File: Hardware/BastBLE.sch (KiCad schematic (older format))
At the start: 35 parts, among them J1 Battery, J2 SWD, J3 Conn_left, J4 Conn_right, P1 USB_C_Plug_USB2.0, Q1 DMG3415U-7, SW1 RESET, U1 AP2112K-3.3, U2 E73-2G4M08S1C, U3 MCP73831-2-OT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

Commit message: Manf#
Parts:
- C1, C2, C3, C4, C5, C6, C7, C8, D2, D3, SW1: manf# (none) -> -
- C10, C9: manf# (none) -> 06035A220JAT4A
- D1: manf# (none) -> MBR120VLSFT3G
- P1: manf# (none) -> MLJ1608WR16JT000
- Q1: manf# (none) -> DMG3415U-7
- R1, R2, R5, R6: manf# (none) -> CRCW0603100KFKEAC
- R3: manf# (none) -> SFR03EZPF4701
- R4, R7: manf# (none) -> RC0603FR-131K27L
- R8, R9: manf# (none) -> CRCW06035K10FKEAC
- U1: manf# (none) -> AP2112K-3.3TRG1
- U3: manf# (none) -> MCP73831-3-OT
- U4: manf# (none) -> W25Q16JVSNIQ
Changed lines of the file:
@@
 EESchema Schematic File Version 4
+LIBS:BastBLE-cache
 EELAYER 30 0
 EELAYER END
@@
 F 2 "Package_TO_SOT_SMD:SOT-23-5" H 1965 6325 50  0001 C CNN
 F 3 "https://www.diodes.com/assets/Datasheets/AP2112.pdf" H 1965 6100 50  0001 C CNN
+F 4 "AP2112K-3.3TRG1" H 1965 6000 50  0001 C CNN "manf#"
 	1    1965 6000
 	1    0    0    -1
@@
 F 2 "Resistor_SMD:R_0603_1608Metric_Pad1.05x0.95mm_HandSolder" H 1490 6040 50  0001 C CNN
 F 3 "~" H 1490 6040 50  0001 C CNN
+F 4 "CRCW0603100KFKEAC" H 1490 6040 50  0001 C CNN "manf#"
 	1    1490 6040
 	1    0    0    -1
@@
 F 2 "Resistor_SMD:R_0603_1608Metric_Pad1.05x0.95mm_HandSolder" H 845 6075 50  0001 C CNN
 F 3 "~" H 845 6075 50  0001 C CNN
+F 4 "CRCW0603100KFKEAC" H 845 6075 50  0001 C CNN "manf#"
 	1    845  6075
 	1    0    0    -1
@@
 F 2 "Diode_SMD:D_SOD-123F" H 1055 5725 50  0001 C CNN
 F 3 "http://www.onsemi.com/pub_link/Collateral/MBR340-D.PDF" H 1055 5900 50  0001 C CNN
+F 4 "MBR120VLSFT3G" H 1055 5900 50  0001 C CNN "manf#"
 	1    1055 5900
 	-1   0    0    1
@@
 F 2 "Capacitor_SMD:C_0603_1608Metric_Pad1.05x0.95mm_HandSolder" H 1290 6070 50  0001 C CNN
 F 3 "~" H 1290 6070 50  0001 C CNN
+F 4 "-" H 1290 6070 50  0001 C CNN "manf#"
 	1    1290 6070
 	1    0    0    -1
@@
 F 2 "Capacitor_SMD:C_0603_1608Metric_Pad1.05x0.95mm_HandSolder" H 2390 6030 50  0001 C CNN
 F 3 "~" H 2390 6030 50  0001 C CNN
+F 4 "-" H 2390 6030 50  0001 C CNN "manf#"
 	1    2390 6030
 	1    0    0    -1
@@
 F 2 "Resistor_SMD:R_0603_1608Metric_Pad1.05x0.95mm_HandSolder" H 4720 865 50  0001 C CNN
 F 3 "~" H 4720 865 50  0001 C CNN
+F 4 "RC0603FR-131K27L" H 4720 865 50  0001 C CNN "manf#"
 	1    4720 865
 	1    0    0    -1
@@
 F 2 "LED_SMD:LED_0805_2012Metric" H 4720 1170 50  0001 C CNN
 F 3 "~" H 4720 1170 50  0001 C CNN
+F 4 "-" H 4720 1170 50  0001 C CNN "manf#"
 	1    4720 1170
 	0    -1   -1   0
@@
 F 2 "Resistor_SMD:R_0603_1608Metric_Pad1.05x0.95mm_HandSolder" H 4720 6695 50  0001 C CNN
 F 3 "~" H 4720 6695 50  0001 C CNN
+F 4 "CRCW0603100KFKEAC" H 4720 6695 50  0001 C CNN "manf#"
 	1    4720 6695
 	1    0    0    -1
@@
 F 2 "Resistor_SMD:R_0603_1608Metric_Pad1.05x0.95mm_HandSolder" H 4720 7020 50  0001 C CNN
 F 3 "~" H 4720 7020 50  0001 C CNN
+F 4 "CRCW0603100KFKEAC" H 4720 7020 50  0001 C CNN "manf#"
 	1    4720 7020
 	1    0    0    -1
@@
 F 2 "Connectors_ElectronicCats:C393939" H 5285 3120 50  0001 C CNN
 F 3 "https://www.usb.org/sites/default/files/documents/usb_type-c.zip" H 5285 3120 50  0001 C CNN
+F 4 "MLJ1608WR16JT000" H 5135 3120 50  0001 C CNN "manf#"
 	1    5135 3120
 	1    0    0    -1
@@
 F 2 "Package_SO:SOIC-8_5.23x5.23mm_P1.27mm" H 8865 5500 50  0001 C CNN
 F 3 "http://www.winbond.com/resource-files/w25q32jv%20revg%2003272018%20plus.pdf" H 8865 5500 50  0001 C CNN
+F 4 "W25Q16JVSNIQ" H 8865 5500 50  0001 C CNN "manf#"
 	1    8865 5500
 	1    0    0    -1
@@
 F 2 "Capacitor_SMD:C_0603_1608Metric_Pad1.05x0.95mm_HandSolder" H 5400 1080 50  0001 C CNN
 F 3 "~" H 5400 1080 50  0001 C CNN
+F 4 "-" H 5400 1080 50  0001 C CNN "manf#"
 	1    5400 1080
 	1    0    0    -1
@@
 F 2 "Capacitor_SMD:C_0603_1608Metric_Pad1.05x0.95mm_HandSolder" H 5740 1075 50  0001 C CNN
 F 3 "~" H 5740 1075 50  0001 C CNN
+F 4 "-" H 5740 1075 50  0001 C CNN "manf#"
 	1    5740 1075
 	1    0    0    -1
@@
 F 2 "Capacitor_SMD:C_0603_1608Metric_Pad1.05x0.95mm_HandSolder" H 6005 1085 50  0001 C CNN
 F 3 "~" H 6005 1085 50  0001 C CNN
+F 4 "-" H 6005 1085 50  0001 C CNN "manf#"
 	1    6005 1085
 	1    0    0    -1
@@
 F 2 "Capacitor_SMD:C_0603_1608Metric_Pad1.05x0.95mm_HandSolder" H 6265 1095 50  0001 C CNN
 F 3 "~" H 6265 1095 50  0001 C CNN
+F 4 "-" H 6265 1095 50  0001 C CNN "manf#"
 	1    6265 1095
 	1    0    0    -1
@@
 F 2 "Capacitor_SMD:C_0603_1608Metric_Pad1.05x0.95mm_HandSolder" H 6535 1095 50  0001 C CNN
 F 3 "~" H 6535 1095 50  0001 C CNN
+F 4 "-" H 6535 1095 50  0001 C CNN "manf#"
 	1    6535 1095
 	1    0    0    -1
@@
 F 2 "Button_Switch_SMD:SW_SPST_TL3342" H 7380 1295 50  0001 C CNN
 F 3 "TS-1185EC-C-D-B" H 7380 1295 50  0001 C CNN
+F 4 "-" H 7380 1095 50  0001 C CNN "manf#"
 	1    7380 1095
 	1    0    0    -1
@@
 F 2 "Resistor_SMD:R_0603_1608Metric_Pad1.05x0.95mm_HandSolder" H 5915 2720 50  0001 C CNN
 F 3 "~" H 5915 2720 50  0001 C CNN
+F 4 "CRCW06035K10FKEAC" H 5915 2720 50  0001 C CNN "manf#"
 	1    5915 2720
 	0    1    1    0
@@
 F 2 "Resistor_SMD:R_0603_1608Metric_Pad1.05x0.95mm_HandSolder" H 5915 2820 50  0001 C CNN
 F 3 "~" H 5915 2820 50  0001 C CNN
+F 4 "CRCW06035K10FKEAC" H 5915 2820 50  0001 C CNN "manf#"
 	1    5915 2820
 	0    1    1    0
@@
 F 2 "Package_TO_SOT_SMD:SOT-23" H 1390 5740 50  0001 C CNN
 F 3 "~" H 1190 5640 50  0001 C CNN
+F 4 "DMG3415U-7" H 1190 5640 50  0001 C CNN "manf#"
 	1    1190 5640
 	1    0    0    -1
@@
 F 2 "Capacitor_SMD:C_0603_1608Metric_Pad1.05x0.95mm_HandSolder" H 4745 5035 50  0001 C CNN
 F 3 "~" H 4745 5035 50  0001 C CNN
+F 4 "-" H 4745 5035 50  0001 C CNN "manf#"
 	1    4745 5035
 	1    0    0    -1
@@
 F 2 "Resistor_SMD:R_0603_1608Metric_Pad1.05x0.95mm_HandSolder" H 3745 5505 50  0001 C CNN
 F 3 "~" H 3745 5505 50  0001 C CNN
+F 4 "SFR03EZPF4701" H 3745 5505 50  0001 C CNN "manf#"
 	1    3745 5505
 	1    0    0    -1
@@
 F 2 "Resistor_SMD:R_0603_1608Metric_Pad1.05x0.95mm_HandSolder" H 4840 5405 50  0001 C CNN
 F 3 "~" H 4840 5405 50  0001 C CNN
+F 4 "RC0603FR-131K27L" H 4840 5405 50  0001 C CNN "manf#"
 	1    4840 5405
 	0    1    1    0
@@
 F 2 "LED_SMD:LED_0805_2012Metric" H 5185 5405 50  0001 C CNN
 F 3 "~" H 5185 5405 50  0001 C CNN
+F 4 "-" H 5185 5405 50  0001 C CNN "manf#"
 	1    5185 5405
 	1    0    0    -1
@@
 F 2 "Package_TO_SOT_SMD:SOT-23-5" H 4320 5055 50  0001 L CIN
 F 3 "http://ww1.microchip.com/downloads/en/DeviceDoc/20001984g.pdf" H 4120 5255 50  0001 C CNN
+F 4 "MCP73831-3-OT" H 4270 5305 50  0001 C CNN "manf#"
 	1    4270 5305
 	1    0    0    -1
@@
 F 2 "Capacitor_SMD:C_0603_1608Metric_Pad1.05x0.95mm_HandSolder" H 1160 2365 50  0001 C CNN
 F 3 "~" H 1160 2365 50  0001 C CNN
+F 4 "06035A220JAT4A" H 1160 2365 50  0001 C CNN "manf#"
 	1    1160 2365
 	0    1    1    0
@@
 F 2 "Capacitor_SMD:C_0603_1608Metric_Pad1.05x0.95mm_HandSolder" H 1160 2030 50  0001 C CNN
 F 3 "~" H 1160 2030 50  0001 C CNN
+F 4 "06035A220JAT4A" H 1160 2030 50  0001 C CNN "manf#"
 	1    1160 2030
 	0    1    1    0

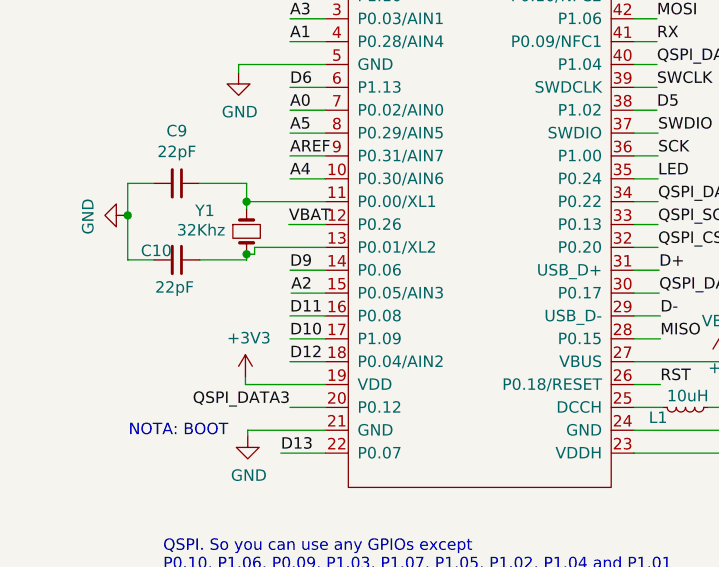
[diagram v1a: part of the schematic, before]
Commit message: VBA and D12 exchanged and routed.
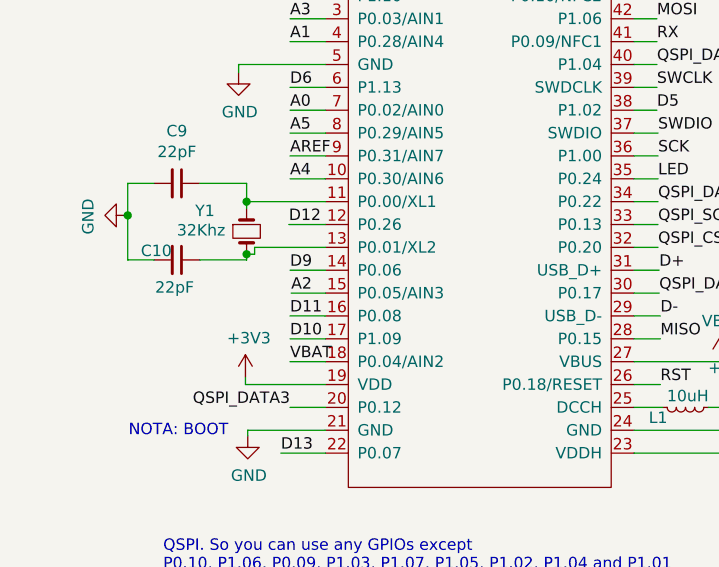
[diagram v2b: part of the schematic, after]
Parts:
- C1, C2, C3, C4, C5, C6, C7, C8, D2, D3, SW1: manf# - -> (none)
- C10, C9: manf# 06035A220JAT4A -> (none)
- D1: manf# MBR120VLSFT3G -> (none)
- P1: manf# MLJ1608WR16JT000 -> (none)
- Q1: manf# DMG3415U-7 -> (none)
- R1, R2, R5, R6: manf# CRCW0603100KFKEAC -> (none)
- R3: manf# SFR03EZPF4701 -> (none)
- R4, R7: manf# RC0603FR-131K27L -> (none)
- R8, R9: manf# CRCW06035K10FKEAC -> (none)
- U1: manf# AP2112K-3.3TRG1 -> (none)
- U3: manf# MCP73831-3-OT -> (none)
- U4: manf# W25Q16JVSNIQ -> (none)
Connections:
- net D12: now also U2.12 (P0.26); no longer U2.18 (P0.04/AIN2)
- net VBAT: now also U2.18 (P0.04/AIN2); no longer U2.12 (P0.26)
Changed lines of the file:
@@
 EESchema Schematic File Version 4
-LIBS:BastBLE-cache
 EELAYER 30 0
 EELAYER END
@@
 F 2 "Package_TO_SOT_SMD:SOT-23-5" H 1965 6325 50  0001 C CNN
 F 3 "https://www.diodes.com/assets/Datasheets/AP2112.pdf" H 1965 6100 50  0001 C CNN
-F 4 "AP2112K-3.3TRG1" H 1965 6000 50  0001 C CNN "manf#"
 	1    1965 6000
 	1    0    0    -1
@@
 F 2 "Resistor_SMD:R_0603_1608Metric_Pad1.05x0.95mm_HandSolder" H 1490 6040 50  0001 C CNN
 F 3 "~" H 1490 6040 50  0001 C CNN
-F 4 "CRCW0603100KFKEAC" H 1490 6040 50  0001 C CNN "manf#"
 	1    1490 6040
 	1    0    0    -1
@@
 RX
 Text Label 1655 2810 0    50   ~ 0
-D12
+VBAT
 Wire Wire Line
 	1615 3210 1810 3210
@@
 F 2 "Resistor_SMD:R_0603_1608Metric_Pad1.05x0.95mm_HandSolder" H 845 6075 50  0001 C CNN
 F 3 "~" H 845 6075 50  0001 C CNN
-F 4 "CRCW0603100KFKEAC" H 845 6075 50  0001 C CNN "manf#"
 	1    845  6075
 	1    0    0    -1
@@
 F 2 "Diode_SMD:D_SOD-123F" H 1055 5725 50  0001 C CNN
 F 3 "http://www.onsemi.com/pub_link/Collateral/MBR340-D.PDF" H 1055 5900 50  0001 C CNN
-F 4 "MBR120VLSFT3G" H 1055 5900 50  0001 C CNN "manf#"
 	1    1055 5900
 	-1   0    0    1
@@
 F 2 "Capacitor_SMD:C_0603_1608Metric_Pad1.05x0.95mm_HandSolder" H 1290 6070 50  0001 C CNN
 F 3 "~" H 1290 6070 50  0001 C CNN
-F 4 "-" H 1290 6070 50  0001 C CNN "manf#"
 	1    1290 6070
 	1    0    0    -1
@@
 F 2 "Capacitor_SMD:C_0603_1608Metric_Pad1.05x0.95mm_HandSolder" H 2390 6030 50  0001 C CNN
 F 3 "~" H 2390 6030 50  0001 C CNN
-F 4 "-" H 2390 6030 50  0001 C CNN "manf#"
 	1    2390 6030
 	1    0    0    -1
@@
 F 2 "Resistor_SMD:R_0603_1608Metric_Pad1.05x0.95mm_HandSolder" H 4720 865 50  0001 C CNN
 F 3 "~" H 4720 865 50  0001 C CNN
-F 4 "RC0603FR-131K27L" H 4720 865 50  0001 C CNN "manf#"
 	1    4720 865
 	1    0    0    -1
@@
 F 2 "LED_SMD:LED_0805_2012Metric" H 4720 1170 50  0001 C CNN
 F 3 "~" H 4720 1170 50  0001 C CNN
-F 4 "-" H 4720 1170 50  0001 C CNN "manf#"
 	1    4720 1170
 	0    -1   -1   0
@@
 F 2 "Resistor_SMD:R_0603_1608Metric_Pad1.05x0.95mm_HandSolder" H 4720 6695 50  0001 C CNN
 F 3 "~" H 4720 6695 50  0001 C CNN
-F 4 "CRCW0603100KFKEAC" H 4720 6695 50  0001 C CNN "manf#"
 	1    4720 6695
 	1    0    0    -1
@@
 F 2 "Resistor_SMD:R_0603_1608Metric_Pad1.05x0.95mm_HandSolder" H 4720 7020 50  0001 C CNN
 F 3 "~" H 4720 7020 50  0001 C CNN
-F 4 "CRCW0603100KFKEAC" H 4720 7020 50  0001 C CNN "manf#"
 	1    4720 7020
 	1    0    0    -1
@@
 Wire Wire Line
 	4720 6855 4720 6795
-Text Label 1650 2210 0    50   ~ 0
-VBAT
 Text Label 4905 6855 0    50   ~ 0
 VBAT
@@
 F 2 "Connectors_ElectronicCats:C393939" H 5285 3120 50  0001 C CNN
 F 3 "https://www.usb.org/sites/default/files/documents/usb_type-c.zip" H 5285 3120 50  0001 C CNN
-F 4 "MLJ1608WR16JT000" H 5135 3120 50  0001 C CNN "manf#"
 	1    5135 3120
 	1    0    0    -1
@@
 F 2 "Package_SO:SOIC-8_5.23x5.23mm_P1.27mm" H 8865 5500 50  0001 C CNN
 F 3 "http://www.winbond.com/resource-files/w25q32jv%20revg%2003272018%20plus.pdf" H 8865 5500 50  0001 C CNN
-F 4 "W25Q16JVSNIQ" H 8865 5500 50  0001 C CNN "manf#"
 	1    8865 5500
 	1    0    0    -1
@@
 F 2 "Capacitor_SMD:C_0603_1608Metric_Pad1.05x0.95mm_HandSolder" H 5400 1080 50  0001 C CNN
 F 3 "~" H 5400 1080 50  0001 C CNN
-F 4 "-" H 5400 1080 50  0001 C CNN "manf#"
 	1    5400 1080
 	1    0    0    -1
@@
 F 2 "Capacitor_SMD:C_0603_1608Metric_Pad1.05x0.95mm_HandSolder" H 5740 1075 50  0001 C CNN
 F 3 "~" H 5740 1075 50  0001 C CNN
-F 4 "-" H 5740 1075 50  0001 C CNN "manf#"
 	1    5740 1075
 	1    0    0    -1
@@
 F 2 "Capacitor_SMD:C_0603_1608Metric_Pad1.05x0.95mm_HandSolder" H 6005 1085 50  0001 C CNN
 F 3 "~" H 6005 1085 50  0001 C CNN
-F 4 "-" H 6005 1085 50  0001 C CNN "manf#"
 	1    6005 1085
 	1    0    0    -1
@@
 F 2 "Capacitor_SMD:C_0603_1608Metric_Pad1.05x0.95mm_HandSolder" H 6265 1095 50  0001 C CNN
 F 3 "~" H 6265 1095 50  0001 C CNN
-F 4 "-" H 6265 1095 50  0001 C CNN "manf#"
 	1    6265 1095
 	1    0    0    -1
@@
 F 2 "Capacitor_SMD:C_0603_1608Metric_Pad1.05x0.95mm_HandSolder" H 6535 1095 50  0001 C CNN
 F 3 "~" H 6535 1095 50  0001 C CNN
-F 4 "-" H 6535 1095 50  0001 C CNN "manf#"
 	1    6535 1095
 	1    0    0    -1
@@
 F 2 "Button_Switch_SMD:SW_SPST_TL3342" H 7380 1295 50  0001 C CNN
 F 3 "TS-1185EC-C-D-B" H 7380 1295 50  0001 C CNN
-F 4 "-" H 7380 1095 50  0001 C CNN "manf#"
 	1    7380 1095
 	1    0    0    -1
@@
 F 2 "Resistor_SMD:R_0603_1608Metric_Pad1.05x0.95mm_HandSolder" H 5915 2720 50  0001 C CNN
 F 3 "~" H 5915 2720 50  0001 C CNN
-F 4 "CRCW06035K10FKEAC" H 5915 2720 50  0001 C CNN "manf#"
 	1    5915 2720
 	0    1    1    0
@@
 F 2 "Resistor_SMD:R_0603_1608Metric_Pad1.05x0.95mm_HandSolder" H 5915 2820 50  0001 C CNN
 F 3 "~" H 5915 2820 50  0001 C CNN
-F 4 "CRCW06035K10FKEAC" H 5915 2820 50  0001 C CNN "manf#"
 	1    5915 2820
 	0    1    1    0
@@
 F 2 "Package_TO_SOT_SMD:SOT-23" H 1390 5740 50  0001 C CNN
 F 3 "~" H 1190 5640 50  0001 C CNN
-F 4 "DMG3415U-7" H 1190 5640 50  0001 C CNN "manf#"
 	1    1190 5640
 	1    0    0    -1
@@
 F 2 "Capacitor_SMD:C_0603_1608Metric_Pad1.05x0.95mm_HandSolder" H 4745 5035 50  0001 C CNN
 F 3 "~" H 4745 5035 50  0001 C CNN
-F 4 "-" H 4745 5035 50  0001 C CNN "manf#"
 	1    4745 5035
 	1    0    0    -1
@@
 F 2 "Resistor_SMD:R_0603_1608Metric_Pad1.05x0.95mm_HandSolder" H 3745 5505 50  0001 C CNN
 F 3 "~" H 3745 5505 50  0001 C CNN
-F 4 "SFR03EZPF4701" H 3745 5505 50  0001 C CNN "manf#"
 	1    3745 5505
 	1    0    0    -1
@@
 F 2 "Resistor_SMD:R_0603_1608Metric_Pad1.05x0.95mm_HandSolder" H 4840 5405 50  0001 C CNN
 F 3 "~" H 4840 5405 50  0001 C CNN
-F 4 "RC0603FR-131K27L" H 4840 5405 50  0001 C CNN "manf#"
 	1    4840 5405
 	0    1    1    0
@@
 F 2 "LED_SMD:LED_0805_2012Metric" H 5185 5405 50  0001 C CNN
 F 3 "~" H 5185 5405 50  0001 C CNN
-F 4 "-" H 5185 5405 50  0001 C CNN "manf#"
 	1    5185 5405
 	1    0    0    -1
@@
 F 2 "Package_TO_SOT_SMD:SOT-23-5" H 4320 5055 50  0001 L CIN
 F 3 "http://ww1.microchip.com/downloads/en/DeviceDoc/20001984g.pdf" H 4120 5255 50  0001 C CNN
-F 4 "MCP73831-3-OT" H 4270 5305 50  0001 C CNN "manf#"
 	1    4270 5305
 	1    0    0    -1
@@
 F 2 "Capacitor_SMD:C_0603_1608Metric_Pad1.05x0.95mm_HandSolder" H 1160 2365 50  0001 C CNN
 F 3 "~" H 1160 2365 50  0001 C CNN
-F 4 "06035A220JAT4A" H 1160 2365 50  0001 C CNN "manf#"
 	1    1160 2365
 	0    1    1    0
@@
 F 2 "Capacitor_SMD:C_0603_1608Metric_Pad1.05x0.95mm_HandSolder" H 1160 2030 50  0001 C CNN
 F 3 "~" H 1160 2030 50  0001 C CNN
-F 4 "06035A220JAT4A" H 1160 2030 50  0001 C CNN "manf#"
 	1    1160 2030
 	0    1    1    0
@@
 	8740 1615 9105 1615
 Connection ~ 8740 1715
+Text Label 1650 2210 0    50   ~ 0
+D12
 $EndSCHEMATC

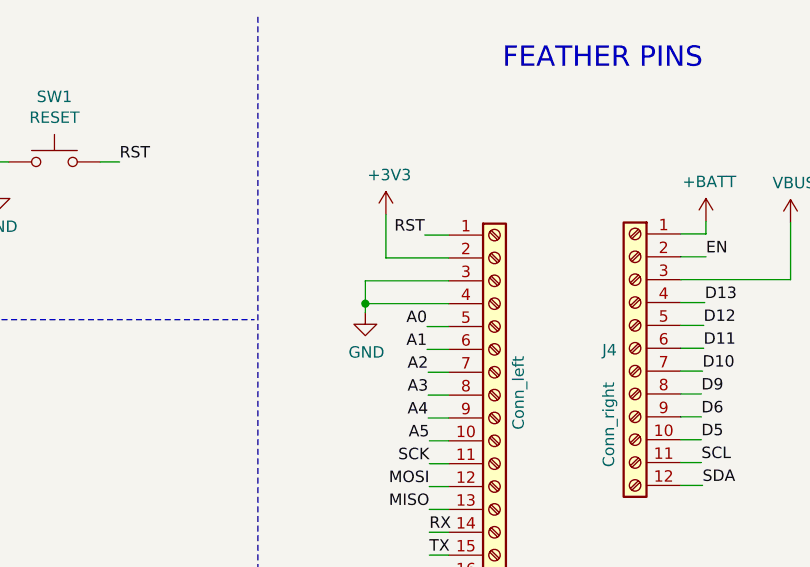
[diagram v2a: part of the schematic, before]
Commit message: AREF routed
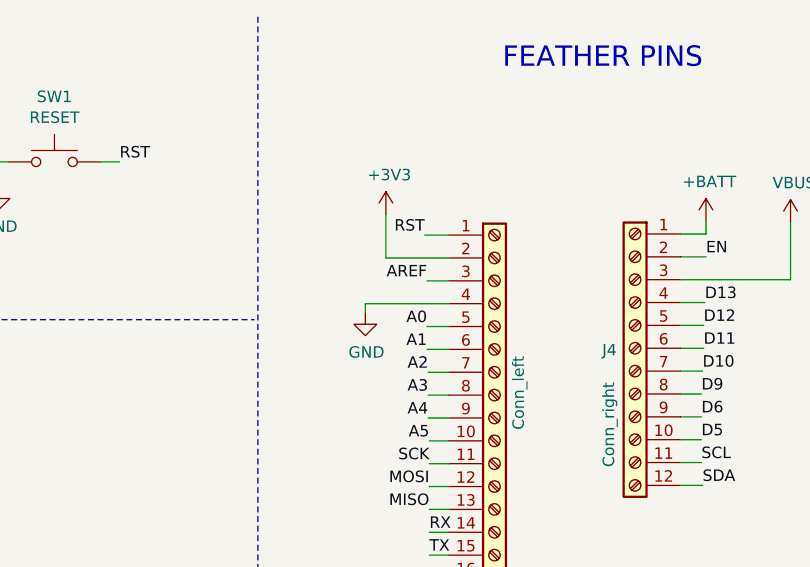
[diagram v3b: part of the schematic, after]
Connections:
- net AREF: now also J3.3 (Pin_3)
- net GND: no longer J3.3 (Pin_3)
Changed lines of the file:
@@
 Text Label 9010 1915 2    50   ~ 0
 A1
-Text Label 9010 1815 2    50   ~ 0
-A0
 Text Label 9000 1415 2    50   ~ 0
 RST
 Wire Wire Line
 	8740 1715 8740 1755
-Wire Wire Line
-	8740 1715 9105 1715
 $Comp
 L power:GND #PWR039
@@
 F 3 "" H 8740 1755 50  0001 C CNN
 	1    8740 1755
-	1    0    0    -1
-$EndComp
-$Comp
-L Connector:Screw_Terminal_01x16 J3
-U 1 1 5E2A6306
-P 9305 2115
-F 0 "J3" H 9223 1090 50  0000 C CNN
-F 1 "Conn_left" V 9410 2125 50  0000 C CNN
-F 2 "Connector_PinHeader_2.54mm:PinHeader_1x16_P2.54mm_Vertical" H 9305 2115 50  0001 C CNN
-F 3 "~" H 9305 2115 50  0001 C CNN
-	1    9305 2115
 	1    0    0    -1
 $EndComp
@@
 Text Label 1655 1310 0    50   ~ 0
 A3
-Wire Wire Line
-	8740 1715 8740 1615
-Wire Wire Line
-	8740 1615 9105 1615
-Connection ~ 8740 1715
 Text Label 1650 2210 0    50   ~ 0
 D12
+$Comp
+L Connector:Screw_Terminal_01x16 J3
+U 1 1 5E2A6306
+P 9305 2115
+F 0 "J3" H 9223 1090 50  0000 C CNN
+F 1 "Conn_left" V 9410 2125 50  0000 C CNN
+F 2 "Connector_PinHeader_2.54mm:PinHeader_1x16_P2.54mm_Vertical" H 9305 2115 50  0001 C CNN
+F 3 "~" H 9305 2115 50  0001 C CNN
+	1    9305 2115
+	1    0    0    -1
+$EndComp
+Wire Wire Line
+	8740 1715 9105 1715
+Text Label 9010 1815 2    50   ~ 0
+A0
+Wire Wire Line
+	9105 1615 9010 1615
+Text Label 9010 1615 2    50   ~ 0
+AREF
 $EndSCHEMATC

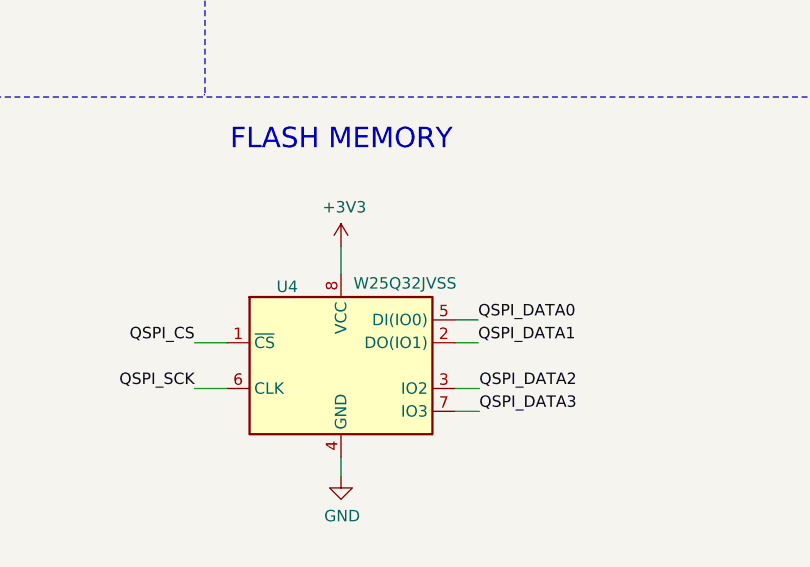
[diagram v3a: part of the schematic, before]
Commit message: change memory GD25Q16C
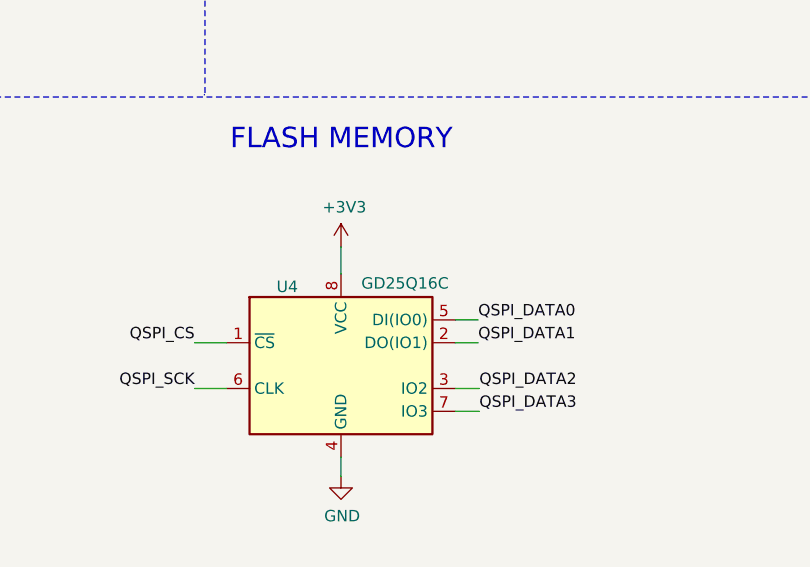
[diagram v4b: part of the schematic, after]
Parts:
- U4: value W25Q32JVSS -> GD25Q16C
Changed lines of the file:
@@
 P 8865 5500
 F 0 "U4" H 8630 5845 50  0000 C CNN
-F 1 "W25Q32JVSS" H 9145 5860 50  0000 C CNN
+F 1 "GD25Q16C" H 9145 5860 50  0000 C CNN
 F 2 "Package_SO:SOIC-8_5.23x5.23mm_P1.27mm" H 8865 5500 50  0001 C CNN
-F 3 "http://www.winbond.com/resource-files/w25q32jv%20revg%2003272018%20plus.pdf" H 8865 5500 50  0001 C CNN
+F 3 "http://www.elm-tech.com/en/products/spi-flash-memory/gd25q16/gd25q16.pdf" H 8865 5500 50  0001 C CNN
 	1    8865 5500
 	1    0    0    -1
